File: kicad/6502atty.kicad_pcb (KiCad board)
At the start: 2 copper layers, 102.7 x 104.7 mm, 104 parts, among them J1 Conn_01x04_Pin, J10 Conn_01x04_Pin, J11 Conn_01x03_Pin, J12 Conn_01x02_Pin, J2 Conn_01x02_Pin, J3 Conn_02x03_Odd_Even, J4 Conn_01x03_Pin, J5 Conn_01x06_Pin, J6 Conn_01x04_Pin, J7 Conn_01x10_Pin, J8 Conn_01x03_Pin, J9 Conn_01x10_Pin, SW1 SW_Push, U1 ATmega164P-20P, U10 74LS08, U11 74LS138, U12 74LS574, U2 74LS112, U3 W65C02SxP, U4 74LS574, U5 74HC245, U6 27C128, U7 KM62256CLP, U8 74LS00, U9 74LS00, Y1 18.432MHz

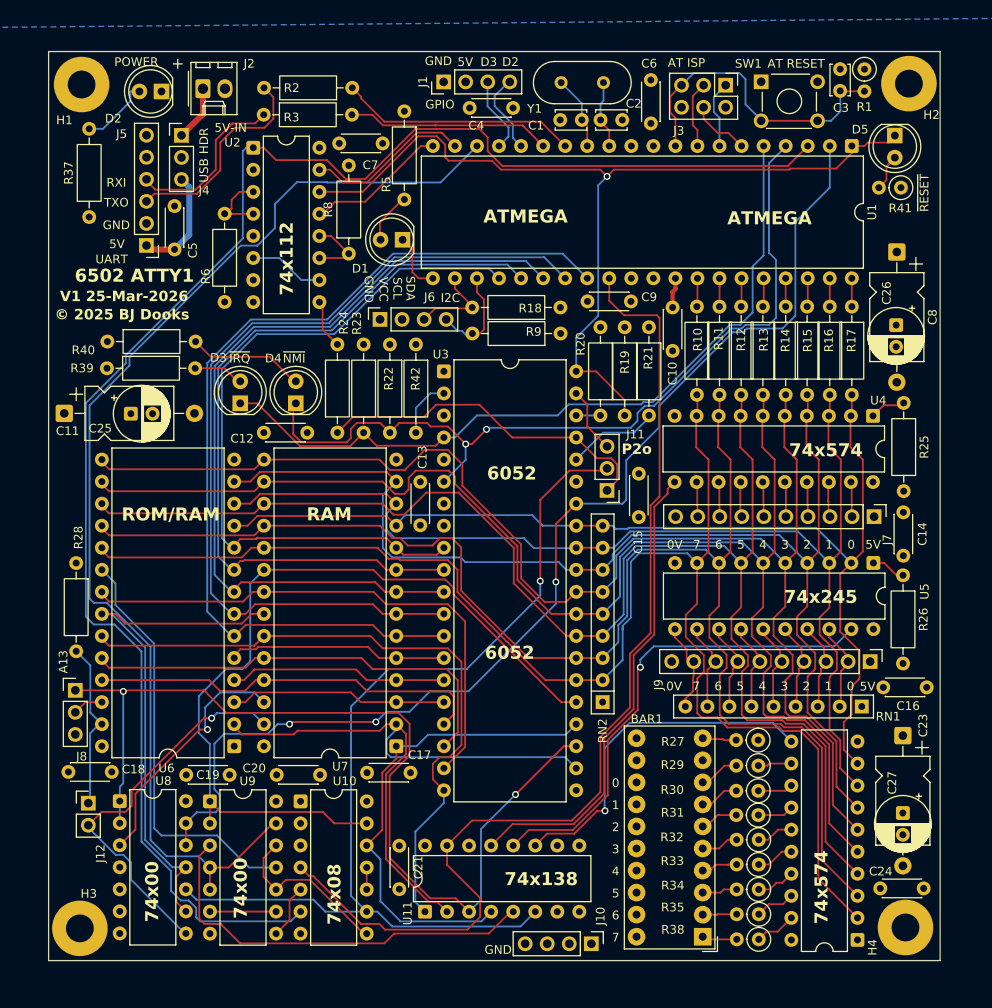
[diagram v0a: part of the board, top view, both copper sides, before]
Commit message: start of rev3, reduce x-size, leds consistent
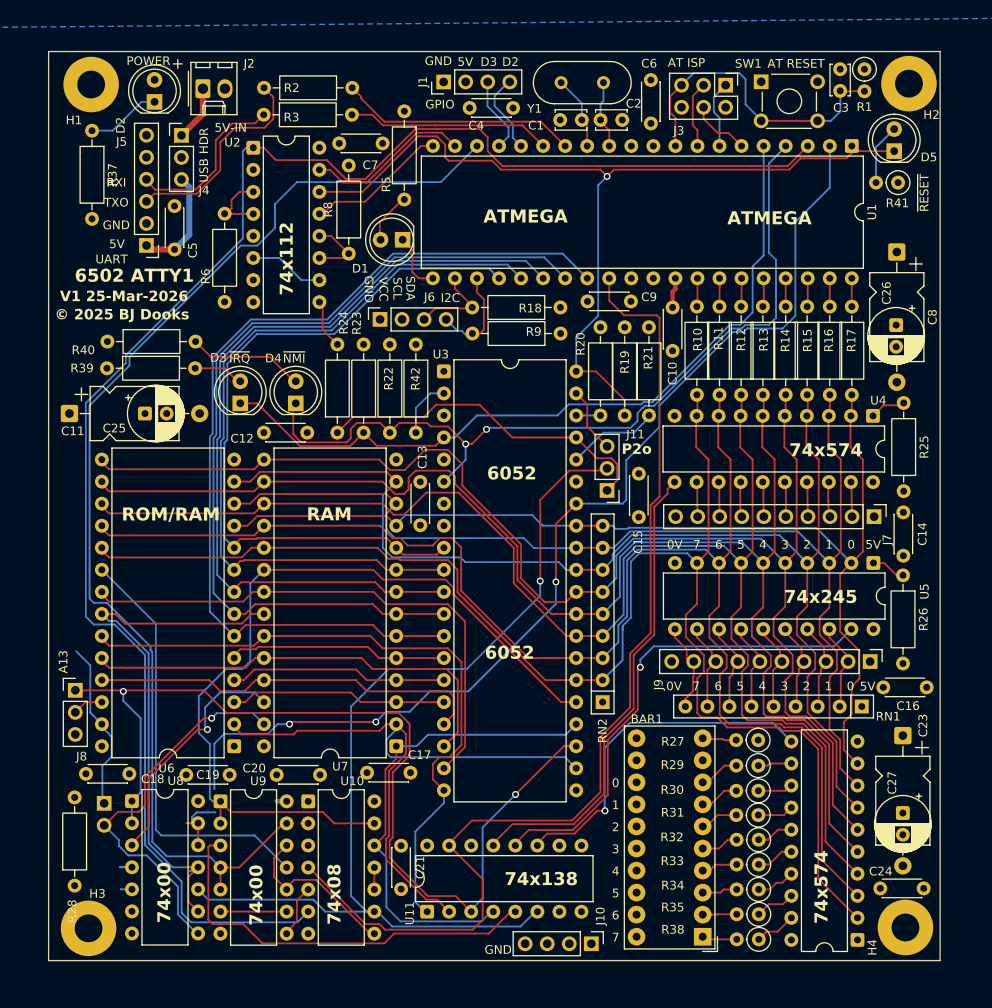
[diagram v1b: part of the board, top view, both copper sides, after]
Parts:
- J12: moved to B.Cu
- RN1: value R_Network08 -> 4K7
- moved R28 37.2 mm to (3.00, 96.2), turned to 90 degrees
- moved R37 9.95 mm to (5.00, 9.22), turned to -90 degrees
- moved C18 2.98 mm to (4.30, 83.3), turned to 0 degrees
- moved J12 1.83 mm to (6.40, 86.7), turned to 180 degrees
- moved D5 1.79 mm to (97.4, 11.6), turned to 90 degrees
- moved C25 1.63 mm to (11.1, 41.8)
- moved D2 1.44 mm to (12.2, 5.90), turned to 90 degrees
- moved U8 1.41 mm to (9.60, 86.4)
- moved U9 1.22 mm to (19.8, 86.5)
- moved H1 1.10 mm to (4.90, 3.90)
- moved H3 1.00 mm to (4.60, 101.1)
- moved U10 0.88 mm to (29.9, 86.5)
- moved R41 0.67 mm to (97.8, 15.2)
- moved C11 0.60 mm to (2.40, 41.8)
- moved U11 0.25 mm to (43.6, 99.2)
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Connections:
- D2 pad 1: GND -> Net-(D2-K)
- D2 pad 2: Net-(D2-A) -> VCC
- R37 pad 1: VCC -> Net-(D2-K)
- R37 pad 2: Net-(D2-A) -> GND
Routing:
- net Net-(D2-K): track 0.00 -> 8.58 mm
- net Net-(D2-A): track 8.21 -> 0.00 mm
- net GND: track 0.45 -> 5.34 mm
- net /~{R}W: track 61.2 -> 64.1 mm
- net Net-(D5-A): track 4.22 -> 7.03 mm
- net /R~{W}: track 132.9 -> 131.4 mm
- net /A13: track 109.4 -> 110.7 mm
- net /~{ROM_CE}: track 48.2 -> 49.4 mm
- net /AT_~{EN}: track 188.4 -> 189.5 mm
- net VCC: track 0.39 -> 1.48 mm
- net /A15: track 95.8 -> 96.5 mm
- net /ROM_SEL: track 134.1 -> 134.7 mm
- net /~{ROM_PGM_WE}: track 19.6 -> 20.2 mm

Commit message: missing save commited
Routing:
- net /~{ROM_PGM_WE}: track 20.2 -> 23.8 mm
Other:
- board size 102.7 x 104.7 mm -> 102 x 104.7 mm

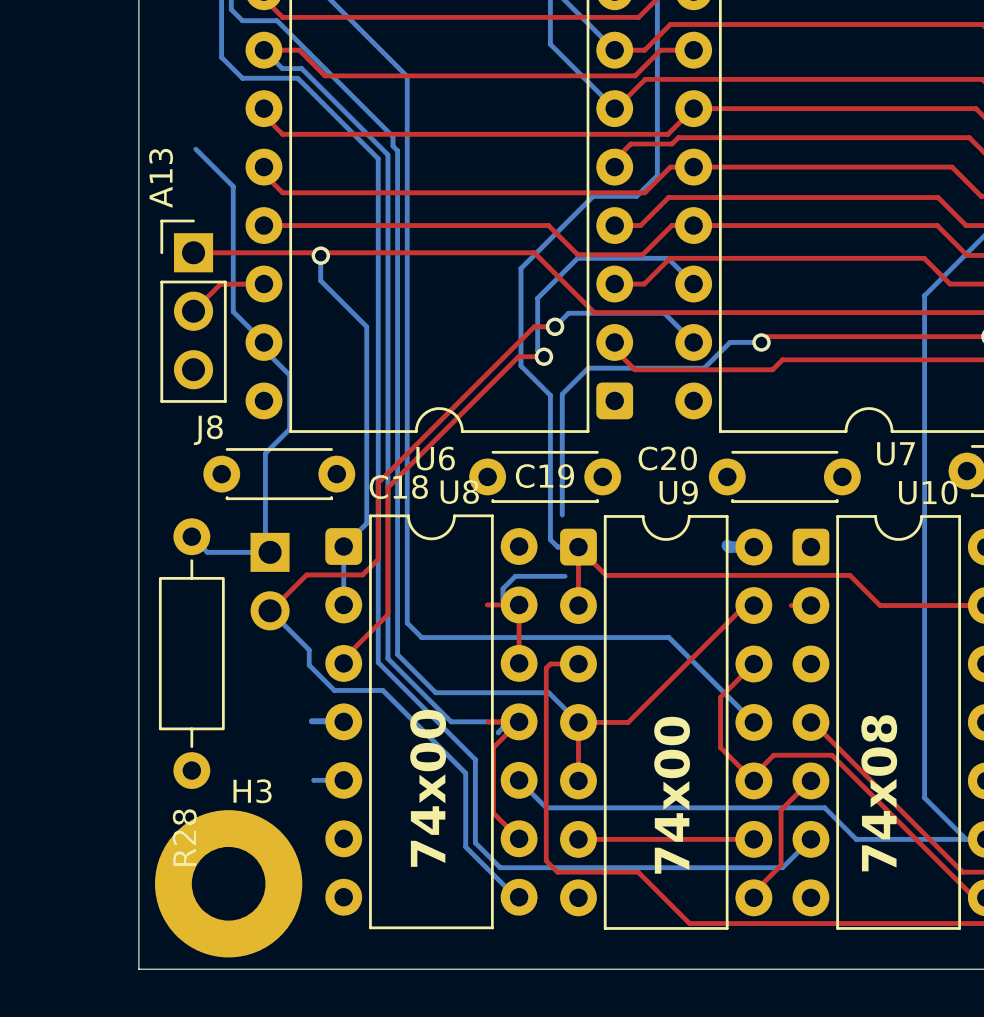
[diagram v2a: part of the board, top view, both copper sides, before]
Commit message: routing fixes and make teardrops slightly smaller
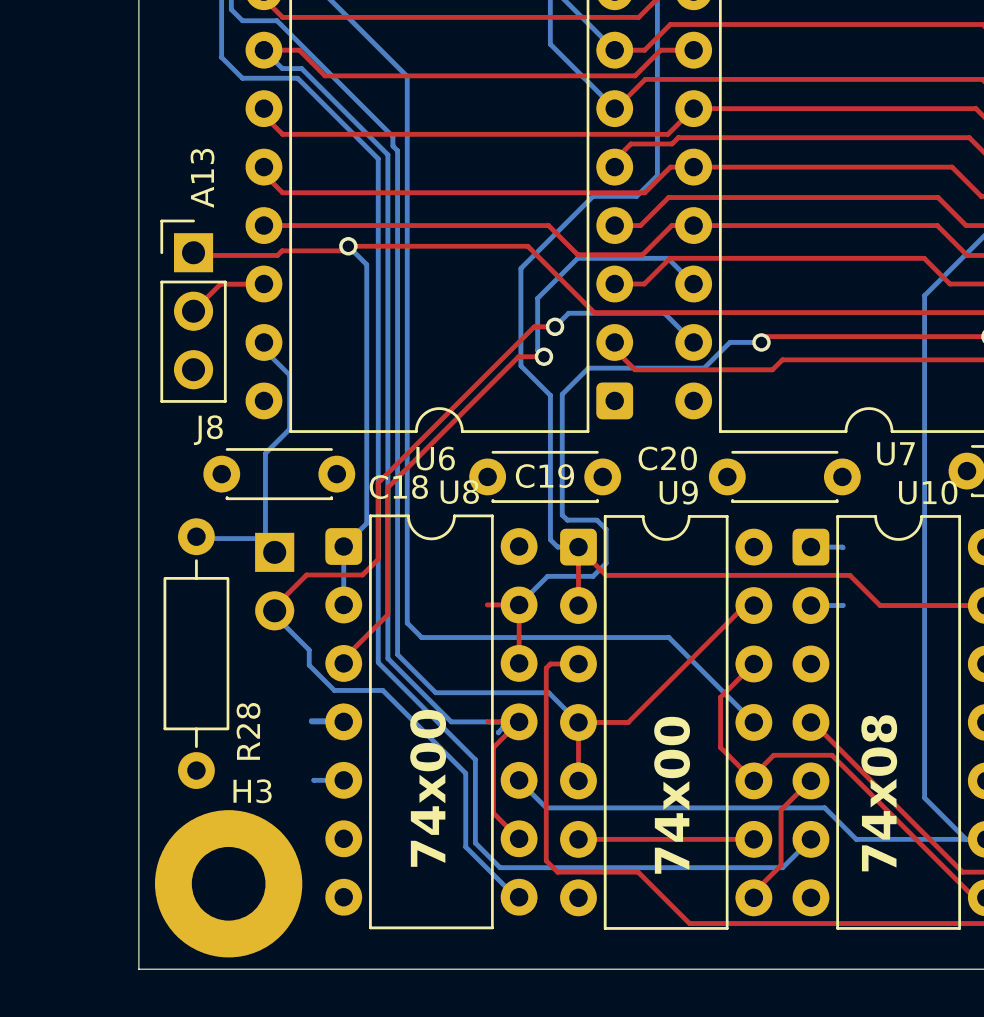
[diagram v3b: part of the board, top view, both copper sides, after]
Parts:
- moved R28 0.20 mm to (3.20, 96.2)
- moved J12 0.20 mm to (6.60, 86.7)
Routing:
- net /~{ROM_PGM_WE}: track 23.8 -> 14.4 mm
- net /R~{W}: track 131.4 -> 135.4 mm
- net GND: track 5.34 -> 7.30 mm
- net VCC: track 1.48 -> 0.30 mm

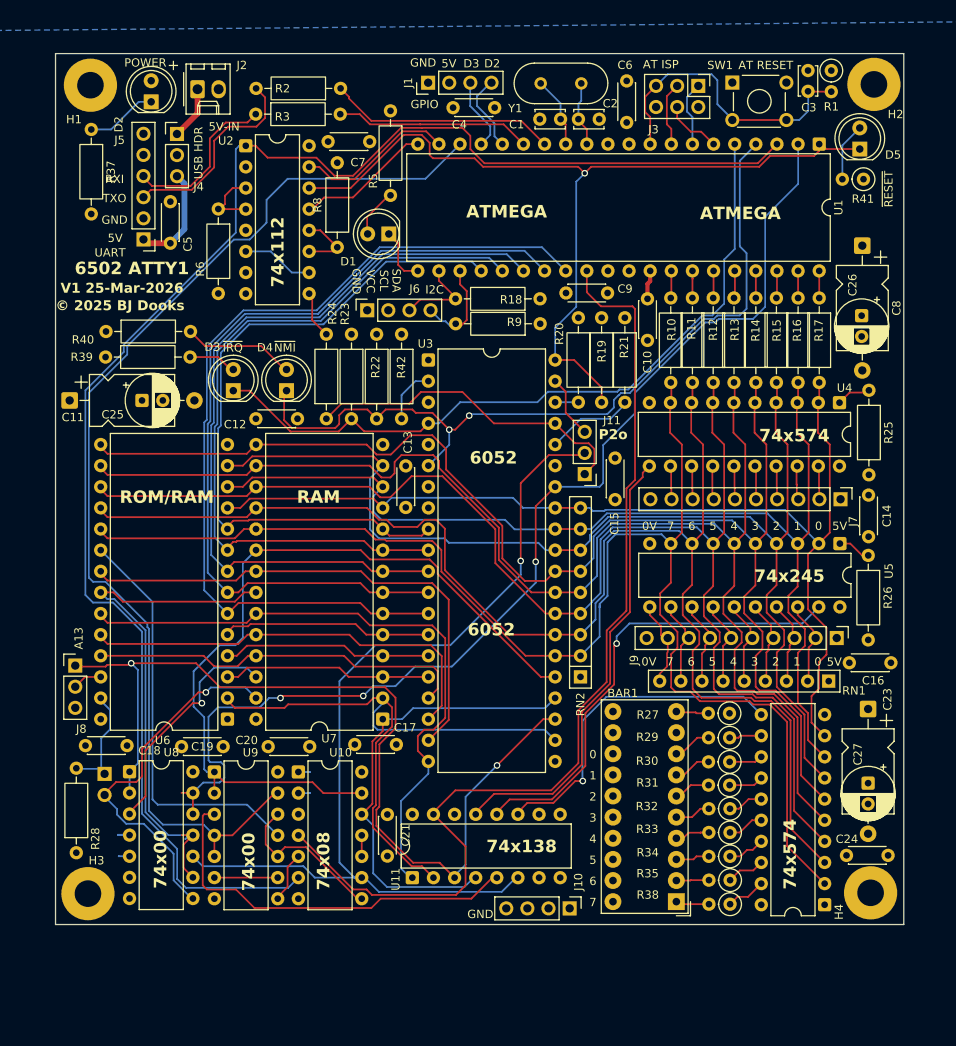
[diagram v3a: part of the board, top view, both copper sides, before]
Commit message: updates for moving pcb stuff around
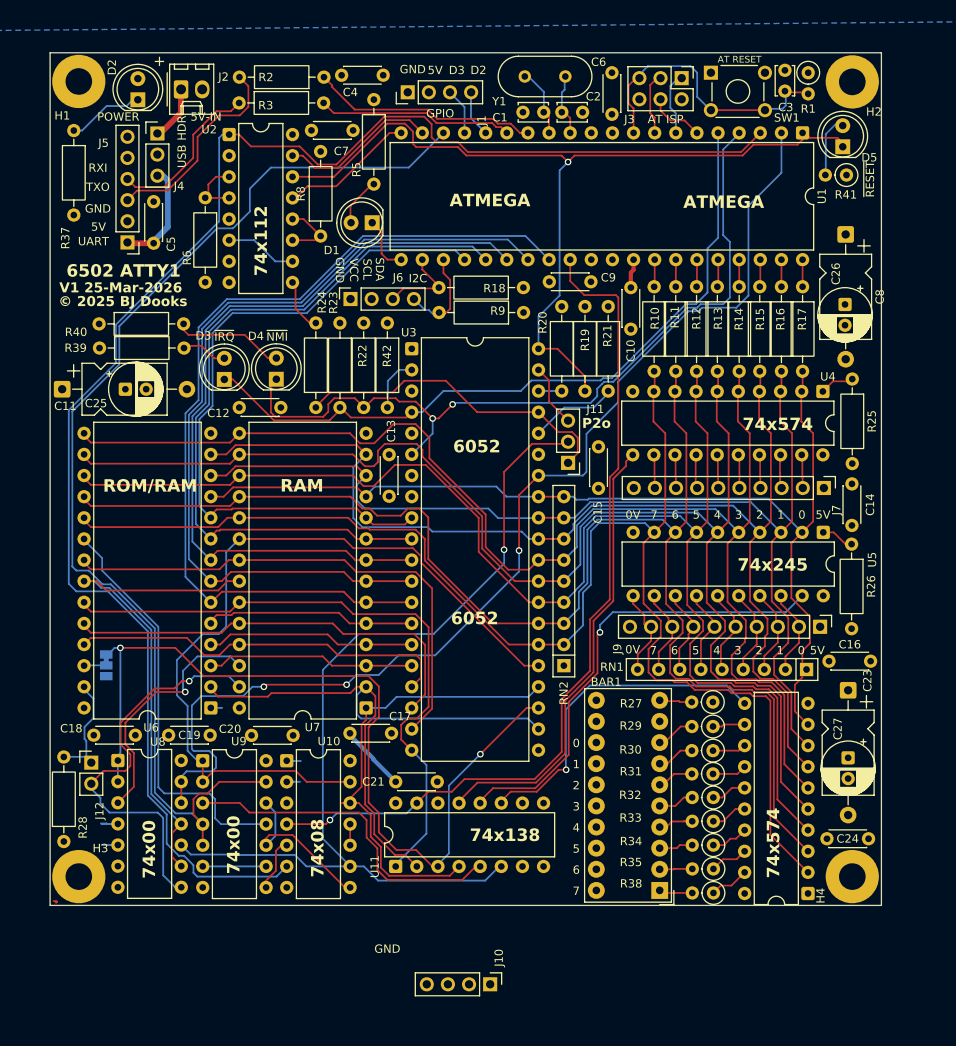
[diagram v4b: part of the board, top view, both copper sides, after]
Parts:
- removed J8: Conn_01x03_Pin, Connector_PinHeader_2.54mm:PinHeader_1x03_P2.54mm_Vertical
- added JP1: SolderJumper_3_Bridged12, Jumper:SolderJumper-3_P1.3mm_Bridged12_Pad1.0x1.5mm_NumberLabels, B.Cu at (6.80, 73.7)
- J12: moved to F.Cu
- moved J10 13.2 mm to (53.0, 112.0)
- moved C4 9.26 mm to (40.1, 2.70), turned to 180 degrees
- moved C21 4.06 mm to (41.6, 87.7), turned to 0 degrees
- moved C27 3.88 mm to (96.0, 84.8)
- moved C23 3.29 mm to (96.0, 76.7)
- moved C24 3.09 mm to (93.5, 94.5)
- moved RN1 3.01 mm to (91.0, 74.2)
- moved H4 2.94 mm to (96.5, 99.0)
- moved SW1 2.83 mm to (79.5, 2.40)
- moved R1 2.79 mm to (91.2, 2.40)
- moved C3 2.77 mm to (88.4, 4.61)
- moved J1 2.71 mm to (43.0, 4.75)
- moved H2 2.62 mm to (96.5, 3.50)
- moved C16 2.45 mm to (93.7, 73.2)
- moved BAR1 2.41 mm to (73.3, 100.7)
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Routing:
- net /AT_~{CE}: track 120.5 -> 103.3 mm, vias 0 -> 1
- net VCC: track 0.30 -> 8.35 mm
- net /control/~{A15}: track 47.8 -> 40.6 mm
- net /A13: track 110.8 -> 104.3 mm
- net /R~{W}ph: track 44.6 -> 49.7 mm
- net /Atmel Controller/PD2: track 9.44 -> 5.62 mm
- net /ROM_SEL: track 134.7 -> 138.1 mm
- net GND: track 7.30 -> 10.6 mm
- net /Atmel Controller/PD3: track 8.85 -> 5.61 mm
- net /~{R}W: track 64.1 -> 60.9 mm
- net /~{A13}: track 28.2 -> 30.2 mm
- net /D3: track 156.4 -> 158.2 mm
- net /Atmel Controller/~{AT_RESET}: track 36.9 -> 35.1 mm
- net /D5: track 162.2 -> 164.0 mm
- net /D2: track 134.8 -> 136.3 mm
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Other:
- board size 102 x 104.7 mm -> 100 x 102.5 mm

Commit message: more movement/updates
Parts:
- moved J10 14.5 mm to (60.9, 99.9)
- moved C1 1.68 mm to (63.2, 7.00)
- moved R2 1.48 mm to (31.8, 2.10)
- moved R3 1.48 mm to (21.6, 5.13)
- moved J1 1.17 mm to (42.2, 3.90)
- moved C4 1.09 mm to (39.0, 2.40)
- moved C2 1.05 mm to (58.4, 7.10)
- moved C11 0.90 mm to (1.50, 39.5)
- moved C14 0.90 mm to (96.5, 50.9)
- moved C16 0.90 mm to (93.7, 72.2)
- moved C20 0.90 mm to (24.3, 81.2)
- moved C21 0.90 mm to (41.6, 86.8)
- moved C23 0.90 mm to (96.0, 75.8)
- moved C24 0.90 mm to (93.5, 93.6)
- moved C25 0.90 mm to (9.10, 39.5)
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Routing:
- net /Atmel Controller/TXD0: track 23.5 -> 26.6 mm
- net /Atmel Controller/RXD0: track 27.4 -> 29.7 mm
- net /A14: track 56.5 -> 55.0 mm
- net GND: track 10.6 -> 12.0 mm
- net /Atmel Controller/~{AT_RESET}: track 35.1 -> 33.8 mm
- net /Atmel Controller/PD2: track 5.62 -> 6.87 mm
- net /CPU_~{NMI}: track 96.7 -> 95.4 mm
- net /Atmel Controller/U_RXI: track 19.7 -> 18.5 mm
- net /Atmel Controller/PD3: track 5.61 -> 6.65 mm
- net /SDA: track 12.5 -> 11.6 mm
- net /ROM_SEL: track 138.1 -> 137.1 mm
- net /Atmel Controller/U_TXO: track 24.9 -> 24.0 mm
- net /Atmel Controller/AT_MOSI: track 6.84 -> 7.65 mm
- net /A0: track 84.3 -> 85.1 mm
- net /AT_~{CE}: track 103.3 -> 102.5 mm
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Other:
- board size 100 x 102.5 mm -> 100 x 101.6 mm
